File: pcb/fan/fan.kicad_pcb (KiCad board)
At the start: 2 copper layers, 234 x 37 mm, 29 parts, among them J1 Conn_01x02_Female, U1 ESP32_DevKit_V1_DOIT, U2 3144_hall_effect_sensor-Sensor

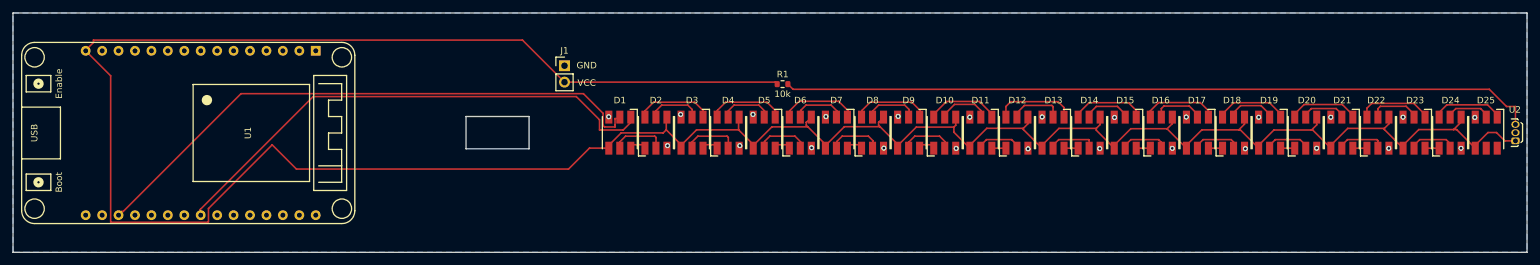
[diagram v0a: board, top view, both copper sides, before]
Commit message: minor adjust length, added solder pads
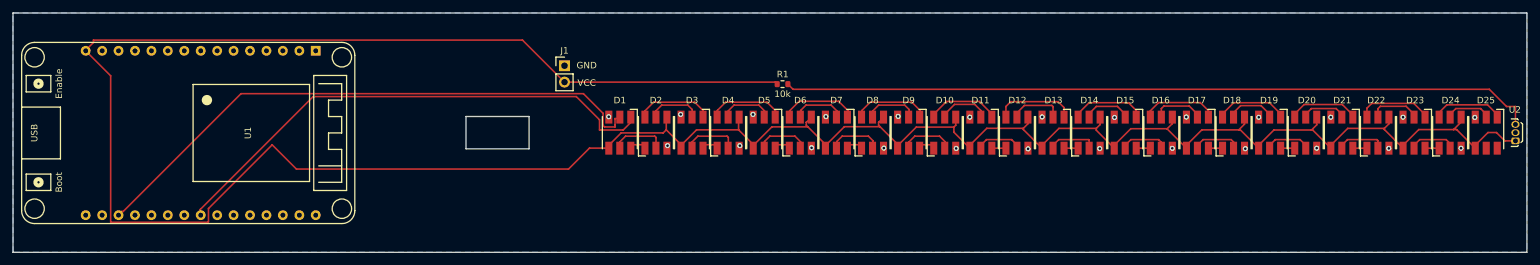
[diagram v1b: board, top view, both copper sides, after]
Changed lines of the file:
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@@
     )
   )
+  (gr_rect (start 222 102.5) (end 276 110.5) (layer "B.Mask") (width 0.15) (fill solid))
+  (gr_rect (start 222 78.5) (end 276 86.5) (layer "B.Mask") (width 0.15) (fill solid))
   (gr_poly
     (pts
-      (xy 283.025 113)
+      (xy 283 113)
       (xy 49.009 113)
       (xy 49 76)
-      (xy 283.025 76)
+      (xy 283 76)
     ) (layer "Edge.Cuts") (width 0.01) (fill none))
   (gr_rect (start 119.025 92) (end 128.775 97) (layer "Edge.Cuts") (width 0.1) (fill none))
@@
     (format (units 3) (units_format 1) (precision 4))
     (style (thickness 0.01) (arrow_length 1.27) (text_position_mode 0) (extension_height 0.58642) (extension_offset 0.5) keep_text_aligned)
+  )
+  (dimension (type aligned) (layer "F.Cu")
+    (pts (xy 49 76) (xy 283 76))
+    (height -22.65)
+    (gr_text "234.0000 mm" (at 166 51.55) (layer "F.Cu")
+      (effects (font (size 1.5 1.5) (thickness 0.3)))
+    )
+    (format (units 3) (units_format 1) (precision 4))
+    (style (thickness 0.2) (arrow_length 1.27) (text_position_mode 0) (extension_height 0.58642) (extension_offset 0.5) keep_text_aligned)
   )
   (segment (start 153.984 96.369) (end 153.984 95.919) (width 0.25) (layer "F.Cu") (net 24))
@@
     (polygon
       (pts
-        (xy 283.025 113)
+        (xy 283 113)
         (xy 49 113)
         (xy 49 76)
-        (xy 283.025 76)
+        (xy 283 76)
       )
     )
